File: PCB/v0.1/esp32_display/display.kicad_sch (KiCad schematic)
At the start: 3 parts, among them U3 Display_ILI9341

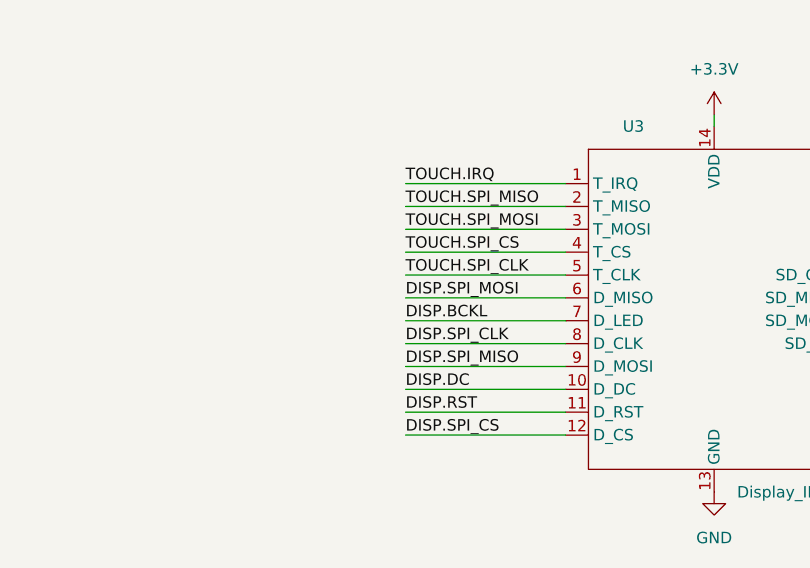
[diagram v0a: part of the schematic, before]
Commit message: Add serial resistors to SPI lines (PCB not finished)
Still missing placment of RC filters.
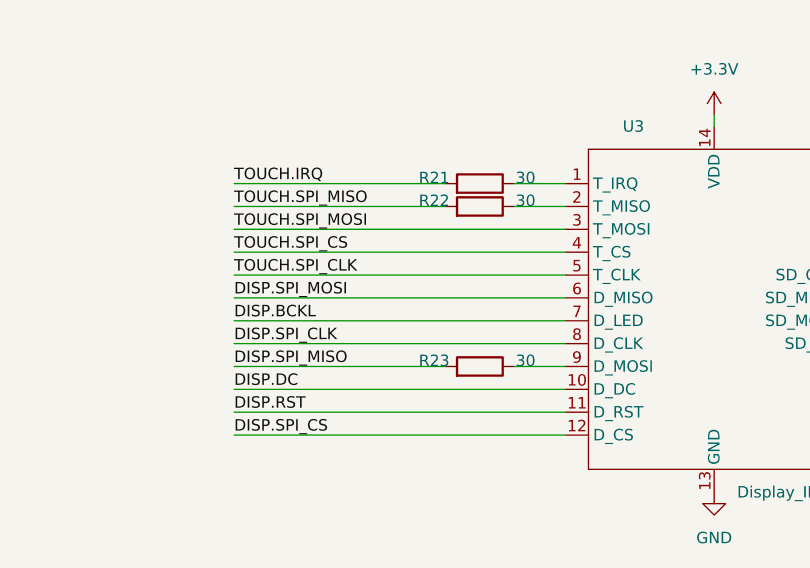
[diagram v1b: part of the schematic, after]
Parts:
- added R21, R22, R23: 30, Resistor_SMD:R_0603_1608Metric_Pad0.98x0.95mm_HandSolder, symbol Device:R
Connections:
- net DISP.SPI_MISO: now also R23.2; no longer U3.9 (D_MOSI)
- net TOUCH.IRQ: now also R21.2; no longer U3.1 (T_IRQ)
- net TOUCH.SPI_MISO: now also R22.2; no longer U3.2 (T_MISO)
- new net: R21.1, U3.1 (T_IRQ)
- new net: R22.1, U3.2 (T_MISO)
- new net: R23.1, U3.9 (D_MOSI)
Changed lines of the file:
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@@
     (stroke (width 0) (type default) (color 0 0 0 0))
   )
-  (wire (pts (xy 104.14 100.33) (xy 121.92 100.33))
+  (wire (pts (xy 85.09 100.33) (xy 121.92 100.33))
     (stroke (width 0) (type default) (color 0 0 0 0))
   )
@@
     (stroke (width 0) (type default) (color 0 0 0 0))
   )
-  (wire (pts (xy 104.14 72.39) (xy 121.92 72.39))
-    (stroke (width 0) (type default) (color 0 0 0 0))
-  )
   (bus (pts (xy 39.37 52.07) (xy 39.37 54.61))
     (stroke (width 0) (type default) (color 0 0 0 0))
@@
     (stroke (width 0) (type default) (color 0 0 0 0))
   )
+  (wire (pts (xy 85.09 72.39) (xy 108.585 72.39))
+    (stroke (width 0) (type default) (color 0 0 0 0))
+  )
   (wire (pts (xy 58.42 33.02) (xy 41.91 33.02))
     (stroke (width 0) (type default) (color 0 0 0 0))
   )
+  (wire (pts (xy 116.205 92.71) (xy 121.92 92.71))
+    (stroke (width 0) (type default) (color 0 0 0 0))
+  )
+  (wire (pts (xy 85.09 74.93) (xy 108.585 74.93))
+    (stroke (width 0) (type default) (color 0 0 0 0))
+  )
   (bus (pts (xy 39.37 35.56) (xy 39.37 38.1))
     (stroke (width 0) (type default) (color 0 0 0 0))
@@
     (stroke (width 0) (type default) (color 0 0 0 0))
   )
-  (wire (pts (xy 104.14 80.01) (xy 121.92 80.01))
+  (wire (pts (xy 85.09 80.01) (xy 121.92 80.01))
     (stroke (width 0) (type default) (color 0 0 0 0))
   )
@@
     (stroke (width 0) (type default) (color 0 0 0 0))
   )
-  (wire (pts (xy 104.14 95.25) (xy 121.92 95.25))
+  (wire (pts (xy 85.09 95.25) (xy 121.92 95.25))
     (stroke (width 0) (type default) (color 0 0 0 0))
   )
@@
     (stroke (width 0) (type default) (color 0 0 0 0))
   )
-  (wire (pts (xy 104.14 74.93) (xy 121.92 74.93))
+  (wire (pts (xy 85.09 92.71) (xy 108.585 92.71))
     (stroke (width 0) (type default) (color 0 0 0 0))
   )
@@
     (stroke (width 0) (type default) (color 0 0 0 0))
   )
-  (wire (pts (xy 104.14 87.63) (xy 121.92 87.63))
-    (stroke (width 0) (type default) (color 0 0 0 0))
-  )
-  (wire (pts (xy 104.14 77.47) (xy 121.92 77.47))
+  (wire (pts (xy 85.09 87.63) (xy 121.92 87.63))
+    (stroke (width 0) (type default) (color 0 0 0 0))
+  )
+  (wire (pts (xy 85.09 77.47) (xy 121.92 77.47))
     (stroke (width 0) (type default) (color 0 0 0 0))
   )
@@
     (stroke (width 0) (type default) (color 0 0 0 0))
   )
-  (wire (pts (xy 104.14 92.71) (xy 121.92 92.71))
-    (stroke (width 0) (type default) (color 0 0 0 0))
-  )
-  (wire (pts (xy 104.14 97.79) (xy 121.92 97.79))
-    (stroke (width 0) (type default) (color 0 0 0 0))
-  )
-  (wire (pts (xy 104.14 90.17) (xy 121.92 90.17))
+  (wire (pts (xy 85.09 97.79) (xy 121.92 97.79))
+    (stroke (width 0) (type default) (color 0 0 0 0))
+  )
+  (wire (pts (xy 85.09 90.17) (xy 121.92 90.17))
     (stroke (width 0) (type default) (color 0 0 0 0))
   )
@@
     (stroke (width 0) (type default) (color 0 0 0 0))
   )
-  (wire (pts (xy 104.14 82.55) (xy 121.92 82.55))
+  (wire (pts (xy 116.205 72.39) (xy 121.92 72.39))
+    (stroke (width 0) (type default) (color 0 0 0 0))
+  )
+  (wire (pts (xy 85.09 82.55) (xy 121.92 82.55))
     (stroke (width 0) (type default) (color 0 0 0 0))
   )
@@
     (stroke (width 0) (type default) (color 0 0 0 0))
   )
-  (wire (pts (xy 104.14 85.09) (xy 121.92 85.09))
+  (wire (pts (xy 85.09 85.09) (xy 121.92 85.09))
     (stroke (width 0) (type default) (color 0 0 0 0))
   )
@@
     (stroke (width 0) (type default) (color 0 0 0 0))
   )
+  (wire (pts (xy 116.205 74.93) (xy 121.92 74.93))
+    (stroke (width 0) (type default) (color 0 0 0 0))
+  )
   (wire (pts (xy 91.44 38.1) (xy 99.06 38.1))
     (stroke (width 0) (type default) (color 0 0 0 0))
@@
     (effects (font (size 1.27 1.27)) (justify right bottom))
   )
-  (label "TOUCH.SPI_CS" (at 104.14 80.01 0)
-    (effects (font (size 1.27 1.27)) (justify left bottom))
-  )
-  (label "DISP.DC" (at 104.14 95.25 0)
+  (label "TOUCH.SPI_CS" (at 85.09 80.01 0)
+    (effects (font (size 1.27 1.27)) (justify left bottom))
+  )
+  (label "DISP.DC" (at 85.09 95.25 0)
     (effects (font (size 1.27 1.27)) (justify left bottom))
   )
@@
     (effects (font (size 1.27 1.27)) (justify right bottom))
   )
-  (label "TOUCH.IRQ" (at 104.14 72.39 0)
+  (label "TOUCH.IRQ" (at 85.09 72.39 0)
     (effects (font (size 1.27 1.27)) (justify left bottom))
   )
@@
     (effects (font (size 1.27 1.27)) (justify right bottom))
   )
-  (label "DISP.SPI_CS" (at 104.14 100.33 0)
+  (label "DISP.SPI_CS" (at 85.09 100.33 0)
     (effects (font (size 1.27 1.27)) (justify left bottom))
   )
@@
     (effects (font (size 1.27 1.27)) (justify right bottom))
   )
-  (label "DISP.SPI_MOSI" (at 104.14 85.09 0)
-    (effects (font (size 1.27 1.27)) (justify left bottom))
-  )
-  (label "DISP.BCKL" (at 104.14 87.63 0)
+  (label "DISP.SPI_MOSI" (at 85.09 85.09 0)
+    (effects (font (size 1.27 1.27)) (justify left bottom))
+  )
+  (label "DISP.BCKL" (at 85.09 87.63 0)
     (effects (font (size 1.27 1.27)) (justify left bottom))
   )
@@
     (effects (font (size 1.27 1.27)) (justify right bottom))
   )
-  (label "DISP.RST" (at 104.14 97.79 0)
+  (label "DISP.RST" (at 85.09 97.79 0)
     (effects (font (size 1.27 1.27)) (justify left bottom))
   )
@@
     (effects (font (size 1.27 1.27)) (justify right bottom))
   )
-  (label "TOUCH.SPI_CLK" (at 104.14 82.55 0)
+  (label "TOUCH.SPI_CLK" (at 85.09 82.55 0)
     (effects (font (size 1.27 1.27)) (justify left bottom))
   )
@@
     (effects (font (size 1.27 1.27)) (justify right bottom))
   )
-  (label "TOUCH.SPI_MOSI" (at 104.14 77.47 0)
-    (effects (font (size 1.27 1.27)) (justify left bottom))
-  )
-  (label "TOUCH.SPI_MISO" (at 104.14 74.93 0)
+  (label "TOUCH.SPI_MOSI" (at 85.09 77.47 0)
+    (effects (font (size 1.27 1.27)) (justify left bottom))
+  )
+  (label "TOUCH.SPI_MISO" (at 85.09 74.93 0)
     (effects (font (size 1.27 1.27)) (justify left bottom))
   )
@@
     (effects (font (size 1.27 1.27)) (justify right bottom))
   )
-  (label "DISP.SPI_CLK" (at 104.14 90.17 0)
+  (label "DISP.SPI_CLK" (at 85.09 90.17 0)
     (effects (font (size 1.27 1.27)) (justify left bottom))
   )
@@
     (effects (font (size 1.27 1.27)) (justify right bottom))
   )
-  (label "DISP.SPI_MISO" (at 104.14 92.71 0)
+  (label "DISP.SPI_MISO" (at 85.09 92.71 0)
     (effects (font (size 1.27 1.27)) (justify left bottom))
   )
@@
   (symbol (lib_id "power:+3.3V") (at 99.06 30.48 0) (unit 1)
     (in_bom yes) (on_board yes) (fields_autoplaced)
-    (property "Reference" "#PWR032" (id 0) (at 99.06 34.29 0)
+    (property "Reference" "#PWR033" (id 0) (at 99.06 34.29 0)
       (effects (font (size 1.27 1.27)) hide)
     )
@@
   (symbol (lib_id "power:+3.3V") (at 138.43 64.77 0) (unit 1)
     (in_bom yes) (on_board yes) (fields_autoplaced)
-    (property "Reference" "#PWR034" (id 0) (at 138.43 68.58 0)
+    (property "Reference" "#PWR035" (id 0) (at 138.43 68.58 0)
       (effects (font (size 1.27 1.27)) hide)
     )
@@
     (pin "9")
   )
+  (symbol (lib_id "Device:R") (at 112.395 92.71 270) (mirror x) (unit 1)
+    (in_bom yes) (on_board yes)
+    (property "Reference" "R23" (id 0) (at 107.315 92.075 90))
+    (property "Value" "30" (id 1) (at 117.475 92.075 90))
+    (property "Footprint" "Resistor_SMD:R_0603_1608Metric_Pad0.98x0.95mm_HandSolder" (id 2) (at 112.395 94.488 90)
+      (effects (font (size 1.27 1.27)) hide)
+    )
+    (property "Datasheet" "~" (id 3) (at 112.395 92.71 0)
+      (effects (font (size 1.27 1.27)) hide)
+    )
+    (pin "1")
+    (pin "2")
+  )
+  (symbol (lib_id "Device:R") (at 112.395 74.93 270) (mirror x) (unit 1)
+    (in_bom yes) (on_board yes)
+    (property "Reference" "R22" (id 0) (at 107.315 74.295 90))
+    (property "Value" "30" (id 1) (at 117.475 74.295 90))
+    (property "Footprint" "Resistor_SMD:R_0603_1608Metric_Pad0.98x0.95mm_HandSolder" (id 2) (at 112.395 76.708 90)
+      (effects (font (size 1.27 1.27)) hide)
+    )
+    (property "Datasheet" "~" (id 3) (at 112.395 74.93 0)
+      (effects (font (size 1.27 1.27)) hide)
+    )
+    (pin "1")
+    (pin "2")
+  )
   (symbol (lib_id "Device:C") (at 91.44 34.29 0) (unit 1)
     (in_bom yes) (on_board yes) (fields_autoplaced)
@@
   (symbol (lib_id "power:GND") (at 138.43 106.68 0) (unit 1)
     (in_bom yes) (on_board yes) (fields_autoplaced)
-    (property "Reference" "#PWR035" (id 0) (at 138.43 113.03 0)
+    (property "Reference" "#PWR036" (id 0) (at 138.43 113.03 0)
       (effects (font (size 1.27 1.27)) hide)
     )
@@
     (pin "1")
   )
+  (symbol (lib_id "Device:R") (at 112.395 72.39 270) (mirror x) (unit 1)
+    (in_bom yes) (on_board yes)
+    (property "Reference" "R21" (id 0) (at 107.315 71.755 90))
+    (property "Value" "30" (id 1) (at 117.475 71.755 90))
+    (property "Footprint" "Resistor_SMD:R_0603_1608Metric_Pad0.98x0.95mm_HandSolder" (id 2) (at 112.395 74.168 90)
+      (effects (font (size 1.27 1.27)) hide)
+    )
+    (property "Datasheet" "~" (id 3) (at 112.395 72.39 0)
+      (effects (font (size 1.27 1.27)) hide)
+    )
+    (pin "1")
+    (pin "2")
+  )
   (symbol (lib_id "power:GND") (at 99.06 38.1 0) (unit 1)
     (in_bom yes) (on_board yes) (fields_autoplaced)
-    (property "Reference" "#PWR033" (id 0) (at 99.06 44.45 0)
-      (effects (font (size 1.27 1.27)) hide)
-    )
+    (property "Reference" "#PWR034" (id 0) (at 99.06 44.45 0)
+      (effects (font (size 1.27 1.27)) hide)
+    )
